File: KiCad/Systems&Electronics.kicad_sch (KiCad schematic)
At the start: 40 parts, among them U13 AD8495, U14 AD8495, U15 AD8495, U16 AD8495, U3 MAX485E, U4 MAX485E

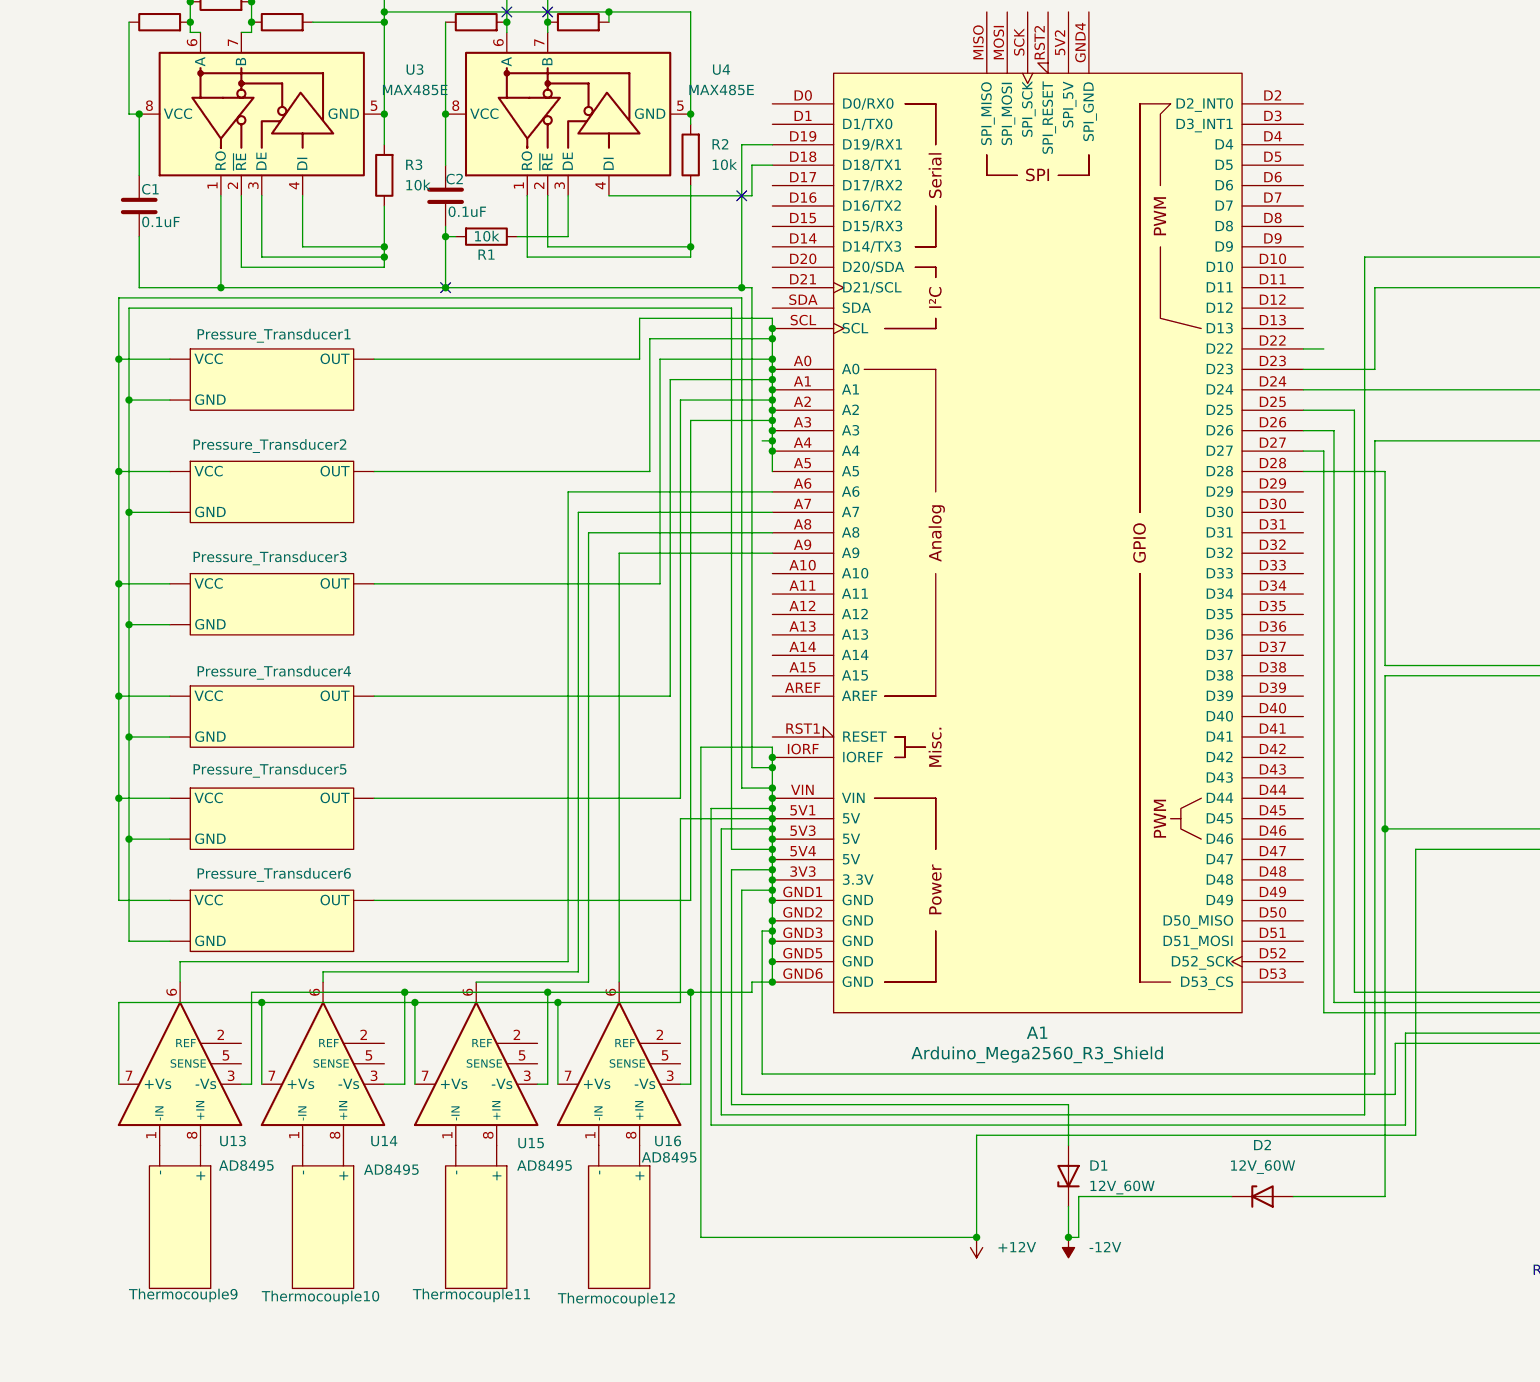
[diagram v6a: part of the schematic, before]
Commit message: Update Systems&Electronics.kicad_sch
Revised version of the added thermocouples
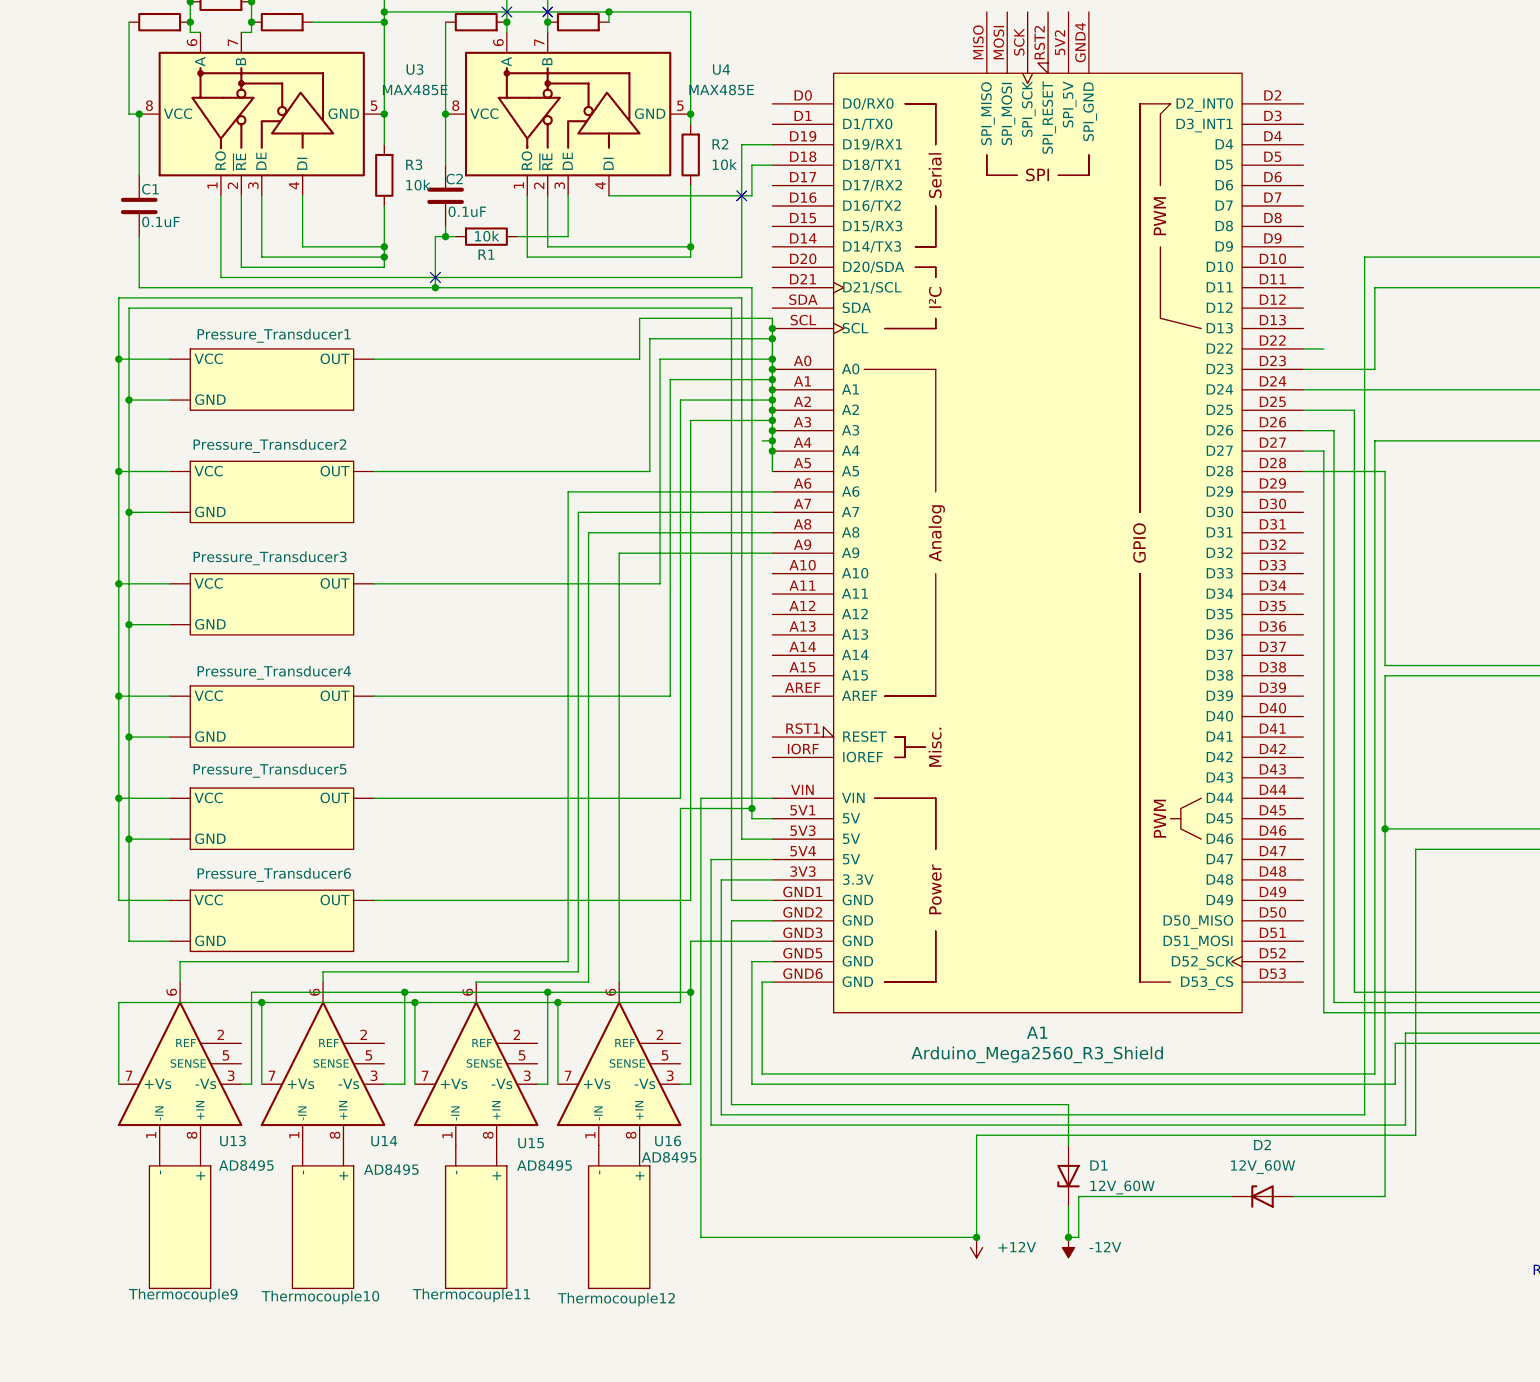
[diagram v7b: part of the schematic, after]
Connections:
- net +12V: no longer A1.3V3 (3.3V), A1.5V1 (5V), A1.5V3 (5V), A1.5V4 (5V), A1.D19 (D19/RX1), A1.GND1 (GND), A1.GND2 (GND), A1.GND3 (GND), A1.GND5 (GND), A1.GND6 (GND), A1.IORF (IOREF), C1.2, C2.1, D1.2 (A), HX711_Board1. (VCC), Pressure_Transducer1. (VCC), Pressure_Transducer2. (VCC), Pressure_Transducer3. (VCC), Pressure_Transducer4. (VCC), Pressure_Transducer5. (VCC), Pressure_Transducer6. (VCC), R1.2, U13.3 (-Vs), U13.7 (+Vs), U14.3 (-Vs), U14.7 (+Vs), U15.3 (-Vs), U15.7 (+Vs), U16.3 (-Vs), U16.7 (+Vs), U3.1 (RO)
- net at Solenoid1. (-): now also D2.2 (A), D3.1 (K), Solenoid2. (-), Solenoid3. (-); no longer 5V Relay1. (NO)
- new net: A1.5V1 (5V), C1.2, C2.1, R1.2, U13.7 (+Vs), U14.7 (+Vs), U15.7 (+Vs), U16.7 (+Vs)
- new net: 5V Relay1. (NO), 5V Relay2. (NO), 5V Relay3. (NO), 5V Relay4. (NO), A1.5V4 (5V)
- new net: 5V Relay1. (NO), 5V Relay2. (NO), 5V Relay3. (NO), 5V Relay4. (NO), A1.GND5 (GND)
- new net: 5V Relay1. (NO), Solenoid1. (-)
- new net: A1.3V3 (3.3V), HX711_Board1. (VCC)
- new net: A1.5V3 (5V), Pressure_Transducer1. (VCC), Pressure_Transducer2. (VCC), Pressure_Transducer3. (VCC), Pressure_Transducer4. (VCC), Pressure_Transducer5. (VCC), Pressure_Transducer6. (VCC)
- new net: A1.D19 (D19/RX1), U3.1 (RO)
- new net: A1.GND1 (GND), Pressure_Transducer1. (VCC), Pressure_Transducer2. (VCC), Pressure_Transducer3. (VCC), Pressure_Transducer4. (VCC), Pressure_Transducer5. (VCC), Pressure_Transducer6. (VCC)
- new net: A1.GND2 (GND), D1.2 (A)
- new net: A1.GND3 (GND), U13.3 (-Vs), U14.3 (-Vs), U15.3 (-Vs), U16.3 (-Vs)
- new net: A1.GND6 (GND), HX711_Board1. (VCC)
- new net: HX711_Board1. (VCC), Load_Cell1. (VCC) (x3)
- new net: 5V Relay3. (NO), Solenoid3. (-)

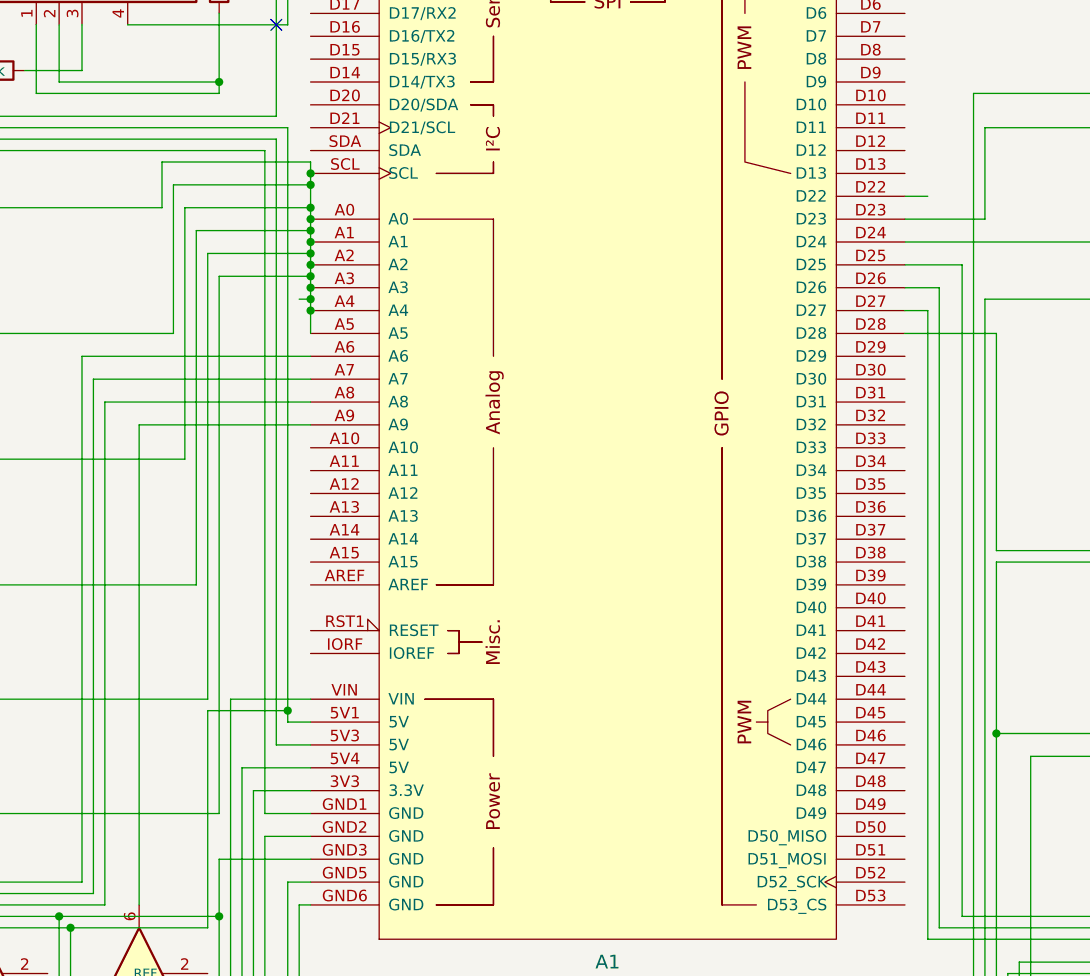
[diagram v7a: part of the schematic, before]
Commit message: fix(schematics): remove shorts in pressure transducers
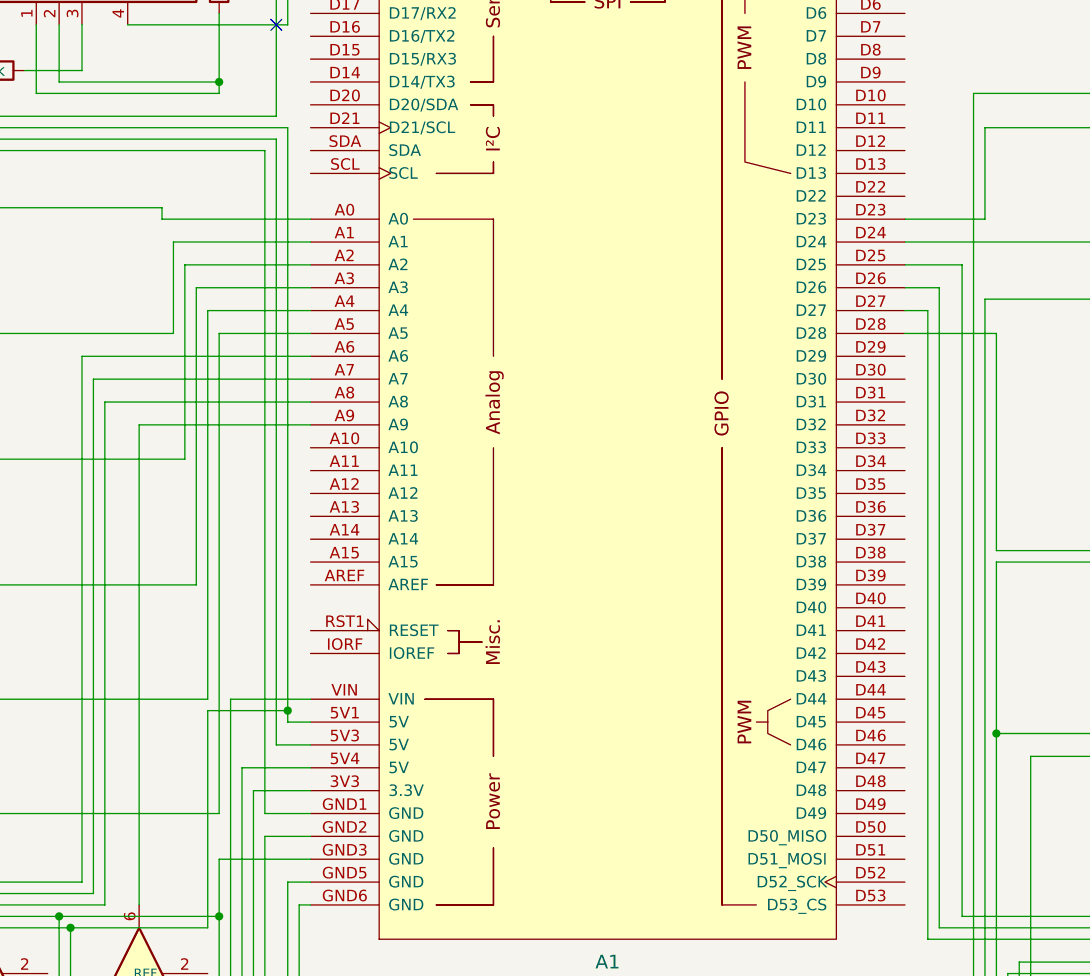
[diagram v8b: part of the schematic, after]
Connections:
- net at Solenoid1. (-): now also D2.2 (A), D3.1 (K), Solenoid2. (-), Solenoid3. (-); no longer 5V Relay1. (NO)
- net at Pressure_Transducer1. (VCC), Pressure_Transducer2. (VCC), Pressure_Transducer3. (VCC)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: now also A1.GND1 (GND); no longer A1.5V3 (5V)
- new net: 5V Relay1. (NO), 5V Relay2. (NO), 5V Relay3. (NO), 5V Relay4. (NO), A1.5V4 (5V)
- new net: 5V Relay1. (NO), 5V Relay2. (NO), 5V Relay3. (NO), 5V Relay4. (NO), A1.GND5 (GND)
- new net: 5V Relay1. (NO), Solenoid1. (-)
- new net: A1.5V3 (5V), Pressure_Transducer1. (VCC), Pressure_Transducer2. (VCC), Pressure_Transducer3. (VCC), Pressure_Transducer4. (VCC), Pressure_Transducer5. (VCC), Pressure_Transducer6. (VCC)
- new net: A1.A0, Pressure_Transducer1. (VCC)
- new net: A1.A1, Pressure_Transducer2. (VCC)
- new net: A1.A2, Pressure_Transducer3. (VCC)
- new net: A1.A3, Pressure_Transducer4. (VCC)
- new net: A1.A4, Pressure_Transducer5. (VCC)
- new net: A1.A5, Pressure_Transducer6. (VCC)
- new net: HX711_Board1. (VCC), Load_Cell1. (VCC) (x3)
- new net: 5V Relay3. (NO), Solenoid3. (-)
- now unconnected: A1.SCL
